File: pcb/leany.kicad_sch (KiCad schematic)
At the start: 40 parts, among them J1 ST7735S, J2 SWD, Q1 AO3401A, SW1 ZERO, SW2 HOLD, SW3 RESET, SW4 FLASH, U1 STM32F103C8Tx, U3 BMI270, U6 CH340N, Y1 8MHz

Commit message: add a reverse-voltage protection mosfet
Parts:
- U6: footprint leany_footprints:SOP-8_3.9x4.9mm_P1.27mm -> Package_SO:JEITA_SOIC-8_3.9x4.9mm_P1.27mm
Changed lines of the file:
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@@
 			)
 		)
-		(property "Footprint" "leany_footprints:SOP-8_3.9x4.9mm_P1.27mm"
+		(property "Footprint" "Package_SO:JEITA_SOIC-8_3.9x4.9mm_P1.27mm"
 			(at 214.63 97.79 0)
 			(effects
@@
 			)
 		)
-		(property "Description" "USB serial converter, 2Mbps, UART, SOP-8"
+		(property "Description" "USB serial converter, 2Mbps, UART, JEITA SOIC-8 (SOP-8)"
 			(at 210.82 116.84 0)
 			(effects

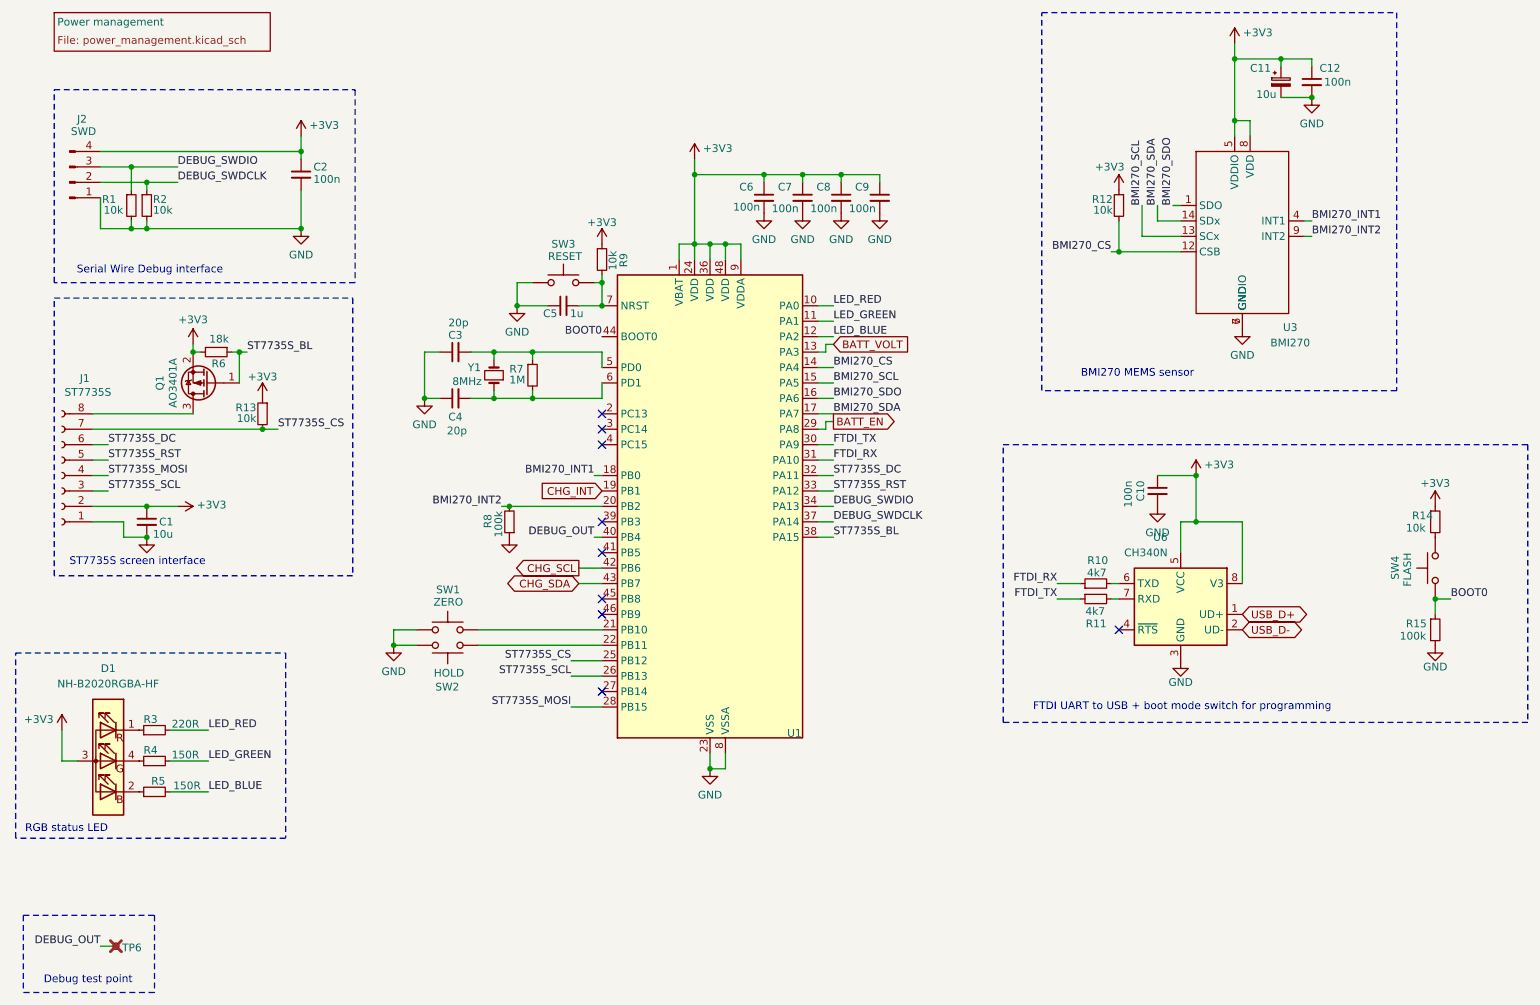
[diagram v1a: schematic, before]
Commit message: replace solder jumper by a test pad near battery
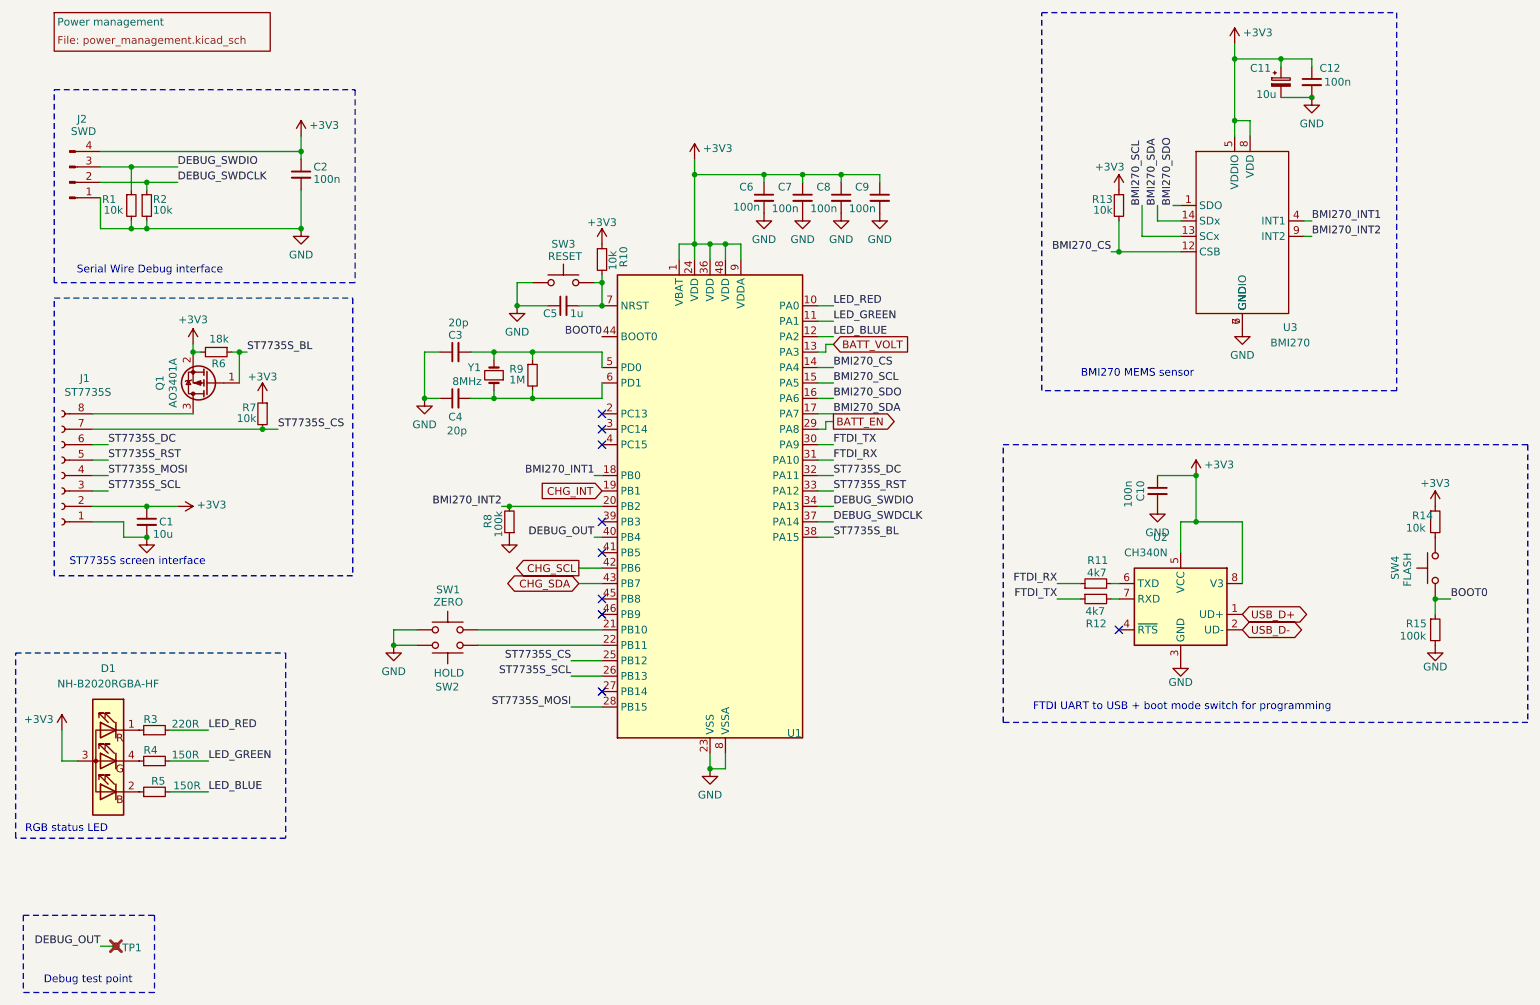
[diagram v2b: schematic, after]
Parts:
- U2: renamed from U6; footprint Package_SO:JEITA_SOIC-8_3.9x4.9mm_P1.27mm -> leany_footprints:SOP-8_3.9x4.9mm_P1.27mm
- renumbered R9 to R10, R10 to R11, R11 to R12, R12 to R13, R13 to R7, R7 to R9, TP6 to TP1
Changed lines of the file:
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@@
 		(on_board yes)
 		(dnp no)
-		(property "Reference" "#PWR06"
+		(property "Reference" "#PWR07"
 			(at 66.04 62.23 0)
 			(effects
@@
 			(project "leany"
 				(path "/e47b2519-93ca-4a48-9414-ecc253dd35f5"
-					(reference "#PWR06")
+					(reference "#PWR07")
 					(unit 1)
 				)
@@
 		(on_board yes)
 		(dnp no)
-		(property "Reference" "#PWR015"
+		(property "Reference" "#PWR016"
 			(at 148.59 59.69 0)
 			(effects
@@
 			(project "leany"
 				(path "/e47b2519-93ca-4a48-9414-ecc253dd35f5"
-					(reference "#PWR015")
+					(reference "#PWR016")
 					(unit 1)
 				)
@@
 		(on_board yes)
 		(dnp no)
-		(property "Reference" "#PWR014"
+		(property "Reference" "#PWR015"
 			(at 142.24 59.69 0)
 			(effects
@@
 			(project "leany"
 				(path "/e47b2519-93ca-4a48-9414-ecc253dd35f5"
-					(reference "#PWR014")
+					(reference "#PWR015")
 					(unit 1)
 				)
@@
 		(on_board yes)
 		(dnp no)
-		(property "Reference" "R12"
+		(property "Reference" "R13"
 			(at 199.644 51.054 0)
 			(effects
@@
 			(project "leany"
 				(path "/e47b2519-93ca-4a48-9414-ecc253dd35f5"
-					(reference "R12")
+					(reference "R13")
 					(unit 1)
 				)
@@
 		(on_board yes)
 		(dnp no)
-		(property "Reference" "#PWR021"
+		(property "Reference" "#PWR022"
 			(at 213.36 100.33 0)
 			(effects
@@
 			(project "leany"
 				(path "/e47b2519-93ca-4a48-9414-ecc253dd35f5"
-					(reference "#PWR021")
+					(reference "#PWR022")
 					(unit 1)
 				)
@@
 		(on_board yes)
 		(dnp no)
-		(property "Reference" "#PWR013"
+		(property "Reference" "#PWR014"
 			(at 133.35 151.13 0)
 			(effects
@@
 			(project ""
 				(path "/e47b2519-93ca-4a48-9414-ecc253dd35f5"
-					(reference "#PWR013")
+					(reference "#PWR014")
 					(unit 1)
 				)
@@
 		(on_board yes)
 		(dnp no)
-		(property "Reference" "#PWR05"
+		(property "Reference" "#PWR06"
 			(at 66.04 44.45 0)
 			(effects
@@
 			(project "leany"
 				(path "/e47b2519-93ca-4a48-9414-ecc253dd35f5"
-					(reference "#PWR05")
+					(reference "#PWR06")
 					(unit 1)
 				)
@@
 		(on_board yes)
 		(dnp no)
-		(property "Reference" "#PWR025"
+		(property "Reference" "#PWR026"
 			(at 252.73 105.41 0)
 			(effects
@@
 			(project "leany"
 				(path "/e47b2519-93ca-4a48-9414-ecc253dd35f5"
-					(reference "#PWR025")
+					(reference "#PWR026")
 					(unit 1)
 				)
@@
 		(on_board yes)
 		(dnp no)
-		(property "Reference" "#PWR018"
+		(property "Reference" "#PWR020"
 			(at 207.01 107.95 0)
 			(effects
@@
 			(project "leany"
 				(path "/e47b2519-93ca-4a48-9414-ecc253dd35f5"
-					(reference "#PWR018")
+					(reference "#PWR020")
 					(unit 1)
 				)
@@
 		(on_board yes)
 		(dnp no)
-		(property "Reference" "#PWR09"
+		(property "Reference" "#PWR011"
 			(at 101.6 74.93 0)
 			(effects
@@
 			(project "leany"
 				(path "/e47b2519-93ca-4a48-9414-ecc253dd35f5"
-					(reference "#PWR09")
+					(reference "#PWR011")
 					(unit 1)
 				)
@@
 		(on_board yes)
 		(dnp no)
-		(property "Reference" "R11"
+		(property "Reference" "R12"
 			(at 198.628 120.904 90)
 			(effects
@@
 			(project "leany"
 				(path "/e47b2519-93ca-4a48-9414-ecc253dd35f5"
-					(reference "R11")
+					(reference "R12")
 					(unit 1)
 				)
@@
 		(on_board yes)
 		(dnp no)
-		(property "Reference" "#PWR045"
+		(property "Reference" "#PWR05"
 			(at 59.69 87.63 0)
 			(effects
@@
 			(project "leany"
 				(path "/e47b2519-93ca-4a48-9414-ecc253dd35f5"
-					(reference "#PWR045")
+					(reference "#PWR05")
 					(unit 1)
 				)
@@
 		(on_board yes)
 		(dnp no)
-		(property "Reference" "#PWR016"
+		(property "Reference" "#PWR017"
 			(at 154.94 59.69 0)
 			(effects
@@
 			(project "leany"
 				(path "/e47b2519-93ca-4a48-9414-ecc253dd35f5"
-					(reference "#PWR016")
+					(reference "#PWR017")
 					(unit 1)
 				)
@@
 		(on_board yes)
 		(dnp no)
-		(property "Reference" "R13"
+		(property "Reference" "R7"
 			(at 58.674 85.344 0)
 			(effects
@@
 			(project "leany"
 				(path "/e47b2519-93ca-4a48-9414-ecc253dd35f5"
-					(reference "R13")
+					(reference "R7")
 					(unit 1)
 				)
@@
 		(on_board yes)
 		(dnp no)
-		(property "Reference" "#PWR07"
+		(property "Reference" "#PWR08"
 			(at 81.28 130.81 0)
 			(effects
@@
 			(project "leany"
 				(path "/e47b2519-93ca-4a48-9414-ecc253dd35f5"
-					(reference "#PWR07")
+					(reference "#PWR08")
 					(unit 1)
 				)
@@
 		(on_board yes)
 		(dnp no)
-		(property "Reference" "R9"
+		(property "Reference" "R10"
 			(at 119.126 62.23 90)
 			(effects
@@
 			(project "leany"
 				(path "/e47b2519-93ca-4a48-9414-ecc253dd35f5"
-					(reference "R9")
+					(reference "R10")
 					(unit 1)
 				)
@@
 		(on_board yes)
 		(dnp no)
-		(property "Reference" "R10"
+		(property "Reference" "R11"
 			(at 198.882 110.49 90)
 			(effects
@@
 			(project "leany"
 				(path "/e47b2519-93ca-4a48-9414-ecc253dd35f5"
-					(reference "R10")
+					(reference "R11")
 					(unit 1)
 				)
@@
 		(on_board yes)
 		(dnp no)
-		(property "Reference" "U6"
+		(property "Reference" "U2"
 			(at 208.6767 106.68 0)
 			(effects
@@
 			)
 		)
-		(property "Footprint" "Package_SO:JEITA_SOIC-8_3.9x4.9mm_P1.27mm"
+		(property "Footprint" "leany_footprints:SOP-8_3.9x4.9mm_P1.27mm"
 			(at 214.63 97.79 0)
 			(effects
@@
 			)
 		)
-		(property "Description" "USB serial converter, 2Mbps, UART, JEITA SOIC-8 (SOP-8)"
+		(property "Description" "USB serial converter, 2Mbps, UART, SOP-8"
 			(at 210.82 116.84 0)
 			(effects
@@
 			(project ""
 				(path "/e47b2519-93ca-4a48-9414-ecc253dd35f5"
-					(reference "U6")
+					(reference "U2")
 					(unit 1)
 				)
@@
 		(on_board yes)
 		(dnp no)
-		(property "Reference" "#PWR023"
+		(property "Reference" "#PWR024"
 			(at 220.98 78.74 0)
 			(effects
@@
 			(project "leany"
 				(path "/e47b2519-93ca-4a48-9414-ecc253dd35f5"
-					(reference "#PWR023")
+					(reference "#PWR024")
 					(unit 1)
 				)
@@
 		(on_board yes)
 		(dnp no)
-		(property "Reference" "R7"
+		(property "Reference" "R9"
 			(at 100.33 78.994 0)
 			(effects
@@
 			(project ""
 				(path "/e47b2519-93ca-4a48-9414-ecc253dd35f5"
-					(reference "R7")
+					(reference "R9")
 					(unit 1)
 				)
@@
 		(on_board yes)
 		(dnp no)
-		(property "Reference" "#PWR08"
+		(property "Reference" "#PWR09"
 			(at 86.36 90.17 0)
 			(effects
@@
 			(project "leany"
 				(path "/e47b2519-93ca-4a48-9414-ecc253dd35f5"
-					(reference "#PWR08")
+					(reference "#PWR09")
 					(unit 1)
 				)
@@
 		(on_board yes)
 		(dnp yes)
-		(property "Reference" "TP6"
+		(property "Reference" "TP1"
 			(at 36.576 174.244 90)
 			(effects
@@
 			(project "leany"
 				(path "/e47b2519-93ca-4a48-9414-ecc253dd35f5"
-					(reference "TP6")
+					(reference "TP1")
 					(unit 1)
 				)
@@
 		(on_board yes)
 		(dnp no)
-		(property "Reference" "#PWR012"
+		(property "Reference" "#PWR013"
 			(at 130.81 48.26 0)
 			(effects
@@
 			(project "leany"
 				(path "/e47b2519-93ca-4a48-9414-ecc253dd35f5"
-					(reference "#PWR012")
+					(reference "#PWR013")
 					(unit 1)
 				)
@@
 		(on_board yes)
 		(dnp no)
-		(property "Reference" "#PWR017"
+		(property "Reference" "#PWR018"
 			(at 161.29 59.69 0)
 			(effects
@@
 			(project "leany"
 				(path "/e47b2519-93ca-4a48-9414-ecc253dd35f5"
-					(reference "#PWR017")
+					(reference "#PWR018")
 					(unit 1)
 				)
@@
 		(on_board yes)
 		(dnp no)
-		(property "Reference" "#PWR020"
+		(property "Reference" "#PWR021"
 			(at 210.82 133.35 0)
 			(effects
@@
 			(project "leany"
 				(path "/e47b2519-93ca-4a48-9414-ecc253dd35f5"
-					(reference "#PWR020")
+					(reference "#PWR021")
 					(unit 1)
 				)
@@
 		(on_board yes)
 		(dnp no)
-		(property "Reference" "#PWR011"
+		(property "Reference" "#PWR012"
 			(at 115.57 62.23 0)
 			(effects
@@
 			(project "leany"
 				(path "/e47b2519-93ca-4a48-9414-ecc253dd35f5"
-					(reference "#PWR011")
+					(reference "#PWR012")
 					(unit 1)
 				)
@@
 		(on_board yes)
 		(dnp no)
-		(property "Reference" "#PWR022"
+		(property "Reference" "#PWR023"
 			(at 219.71 29.21 0)
 			(effects
@@
 			(project "leany"
 				(path "/e47b2519-93ca-4a48-9414-ecc253dd35f5"
-					(reference "#PWR022")
+					(reference "#PWR023")
 					(unit 1)
 				)
@@
 		(on_board yes)
 		(dnp no)
-		(property "Reference" "#PWR024"
+		(property "Reference" "#PWR025"
 			(at 232.41 40.64 0)
 			(effects
@@
 			(project "leany"
 				(path "/e47b2519-93ca-4a48-9414-ecc253dd35f5"
-					(reference "#PWR024")
+					(reference "#PWR025")
 					(unit 1)
 				)
@@
 		(on_board yes)
 		(dnp no)
-		(property "Reference" "#PWR026"
+		(property "Reference" "#PWR027"
 			(at 252.73 130.81 0)
 			(effects
@@
 			(project "leany"
 				(path "/e47b2519-93ca-4a48-9414-ecc253dd35f5"
-					(reference "#PWR026")
+					(reference "#PWR027")
 					(unit 1)
 				)

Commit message: start re-designing PCB to 4 layers
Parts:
- C10, C12, C2, C3, C4, C5, C6, C7, C8, C9: footprint Capacitor_SMD:C_0603_1608Metric -> Capacitor_SMD:C_0402_1005Metric
- R1, R10, R11, R12, R13, R14, R15, R2, R3, R4, R5, R6, R7, R8, R9: footprint Resistor_SMD:R_0603_1608Metric -> Resistor_SMD:R_0402_1005Metric
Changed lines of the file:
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@@
 			)
 		)
-		(property "Footprint" "Resistor_SMD:R_0603_1608Metric"
+		(property "Footprint" "Resistor_SMD:R_0402_1005Metric"
 			(at 252.73 121.92 0)
 			(effects
@@
 			)
 		)
-		(property "Footprint" "Capacitor_SMD:C_0603_1608Metric"
+		(property "Footprint" "Capacitor_SMD:C_0402_1005Metric"
 			(at 161.29 50.8 0)
 			(effects
@@
 			)
 		)
-		(property "Footprint" "Resistor_SMD:R_0603_1608Metric"
+		(property "Footprint" "Resistor_SMD:R_0402_1005Metric"
 			(at 41.91 148.59 0)
 			(effects
@@
 			)
 		)
-		(property "Footprint" "Resistor_SMD:R_0603_1608Metric"
+		(property "Footprint" "Resistor_SMD:R_0402_1005Metric"
 			(at 38.1 52.07 0)
 			(effects
@@
 			)
 		)
-		(property "Footprint" "Resistor_SMD:R_0603_1608Metric"
+		(property "Footprint" "Resistor_SMD:R_0402_1005Metric"
 			(at 40.64 52.07 0)
 			(effects
@@
 			)
 		)
-		(property "Footprint" "Resistor_SMD:R_0603_1608Metric"
+		(property "Footprint" "Resistor_SMD:R_0402_1005Metric"
 			(at 200.66 52.07 0)
 			(effects
@@
 			)
 		)
-		(property "Footprint" "Capacitor_SMD:C_0603_1608Metric"
+		(property "Footprint" "Capacitor_SMD:C_0402_1005Metric"
 			(at 91.44 83.82 0)
 			(effects
@@
 			)
 		)
-		(property "Footprint" "Capacitor_SMD:C_0603_1608Metric"
+		(property "Footprint" "Capacitor_SMD:C_0402_1005Metric"
 			(at 66.04 46.99 0)
 			(effects
@@
 			)
 		)
-		(property "Footprint" "Capacitor_SMD:C_0603_1608Metric"
+		(property "Footprint" "Capacitor_SMD:C_0402_1005Metric"
 			(at 232.41 31.75 0)
 			(effects
@@
 			)
 		)
-		(property "Footprint" "Resistor_SMD:R_0603_1608Metric"
+		(property "Footprint" "Resistor_SMD:R_0402_1005Metric"
 			(at 41.91 143.51 0)
 			(effects
@@
 			)
 		)
-		(property "Footprint" "Resistor_SMD:R_0603_1608Metric"
+		(property "Footprint" "Resistor_SMD:R_0402_1005Metric"
 			(at 252.73 104.14 0)
 			(effects
@@
 			)
 		)
-		(property "Footprint" "Resistor_SMD:R_0603_1608Metric"
+		(property "Footprint" "Resistor_SMD:R_0402_1005Metric"
 			(at 196.85 116.84 0)
 			(effects
@@
 			)
 		)
-		(property "Footprint" "Resistor_SMD:R_0603_1608Metric"
+		(property "Footprint" "Resistor_SMD:R_0402_1005Metric"
 			(at 59.69 86.36 0)
 			(effects
@@
 			)
 		)
-		(property "Footprint" "Resistor_SMD:R_0603_1608Metric"
+		(property "Footprint" "Resistor_SMD:R_0402_1005Metric"
 			(at 52.07 76.2 0)
 			(effects
@@
 			)
 		)
-		(property "Footprint" "Resistor_SMD:R_0603_1608Metric"
+		(property "Footprint" "Resistor_SMD:R_0402_1005Metric"
 			(at 115.57 60.96 0)
 			(effects
@@
 			)
 		)
-		(property "Footprint" "Resistor_SMD:R_0603_1608Metric"
+		(property "Footprint" "Resistor_SMD:R_0402_1005Metric"
 			(at 196.85 114.3 0)
 			(effects
@@
 			)
 		)
-		(property "Footprint" "Capacitor_SMD:C_0603_1608Metric"
+		(property "Footprint" "Capacitor_SMD:C_0402_1005Metric"
 			(at 109.22 68.58 0)
 			(effects
@@
 			)
 		)
-		(property "Footprint" "Resistor_SMD:R_0603_1608Metric"
+		(property "Footprint" "Resistor_SMD:R_0402_1005Metric"
 			(at 104.14 80.01 0)
 			(effects
@@
 			)
 		)
-		(property "Footprint" "Resistor_SMD:R_0603_1608Metric"
+		(property "Footprint" "Resistor_SMD:R_0402_1005Metric"
 			(at 41.91 138.43 0)
 			(effects
@@
 			)
 		)
-		(property "Footprint" "Capacitor_SMD:C_0603_1608Metric"
+		(property "Footprint" "Capacitor_SMD:C_0402_1005Metric"
 			(at 154.94 50.8 0)
 			(effects
@@
 			)
 		)
-		(property "Footprint" "Capacitor_SMD:C_0603_1608Metric"
+		(property "Footprint" "Capacitor_SMD:C_0402_1005Metric"
 			(at 91.44 76.2 0)
 			(effects
@@
 			)
 		)
-		(property "Footprint" "Capacitor_SMD:C_0603_1608Metric"
+		(property "Footprint" "Capacitor_SMD:C_0402_1005Metric"
 			(at 142.24 50.8 0)
 			(effects
@@
 			)
 		)
-		(property "Footprint" "Capacitor_SMD:C_0603_1608Metric"
+		(property "Footprint" "Capacitor_SMD:C_0402_1005Metric"
 			(at 148.59 50.8 0)
 			(effects
@@
 			)
 		)
-		(property "Footprint" "Resistor_SMD:R_0603_1608Metric"
+		(property "Footprint" "Resistor_SMD:R_0402_1005Metric"
 			(at 100.33 104.14 0)
 			(effects
@@
 			)
 		)
-		(property "Footprint" "Capacitor_SMD:C_0603_1608Metric"
+		(property "Footprint" "Capacitor_SMD:C_0402_1005Metric"
 			(at 207.01 99.06 0)
 			(effects

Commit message: start placing components
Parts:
- added C25, C26: 100n, Capacitor_SMD:C_0402_1005Metric, symbol Device:C_Small
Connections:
- net +3V3: now also C25.1, C26.1
- net GND: now also C25.2, C26.2

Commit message: update resistors BOM
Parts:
- R1, R10, R13, R14, R2, R7: LCSC C25804 -> C25744
- R11, R12: LCSC C23162 -> C25900
- R15, R8: LCSC C25803 -> C25741
- R3: LCSC C22962 -> C25091
- R4, R5, R6: footprint Resistor_SMD:R_0402_1005Metric -> Resistor_SMD:R_0603_1608Metric
- R9: LCSC C22935 -> C26083
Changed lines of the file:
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@@
 			)
 		)
-		(property "LCSC" "C25803"
+		(property "LCSC" "C25741"
 			(at 252.73 121.92 0)
 			(effects
@@
 			)
 		)
-		(property "Footprint" "Resistor_SMD:R_0402_1005Metric"
+		(property "Footprint" "Resistor_SMD:R_0603_1608Metric"
 			(at 41.91 148.59 0)
 			(effects
@@
 			)
 		)
-		(property "LCSC" "C25804"
+		(property "LCSC" "C25744"
 			(at 38.1 52.07 0)
 			(effects
@@
 			)
 		)
-		(property "LCSC" "C25804"
+		(property "LCSC" "C25744"
 			(at 40.64 52.07 0)
 			(effects
@@
 			)
 		)
-		(property "LCSC" "C25804"
+		(property "LCSC" "C25744"
 			(at 200.66 52.07 0)
 			(effects
@@
 			)
 		)
-		(property "Footprint" "Resistor_SMD:R_0402_1005Metric"
+		(property "Footprint" "Resistor_SMD:R_0603_1608Metric"
 			(at 41.91 143.51 0)
 			(effects
@@
 			)
 		)
-		(property "LCSC" "C25804"
+		(property "LCSC" "C25744"
 			(at 252.73 104.14 0)
 			(effects
@@
 			)
 		)
-		(property "LCSC" "C23162"
+		(property "LCSC" "C25900"
 			(at 196.85 116.84 0)
 			(effects
@@
 			)
 		)
-		(property "LCSC" "C25804"
+		(property "LCSC" "C25744"
 			(at 59.69 86.36 0)
 			(effects
@@
 			)
 		)
-		(property "Footprint" "Resistor_SMD:R_0402_1005Metric"
+		(property "Footprint" "Resistor_SMD:R_0603_1608Metric"
 			(at 52.07 76.2 0)
 			(effects
@@
 			)
 		)
-		(property "LCSC" "C25804"
+		(property "LCSC" "C25744"
 			(at 115.57 60.96 0)
 			(effects
@@
 			)
 		)
-		(property "LCSC" "C23162"
+		(property "LCSC" "C25900"
 			(at 196.85 114.3 0)
 			(effects
@@
 			)
 		)
-		(property "LCSC" "C22935"
+		(property "LCSC" "C26083"
 			(at 104.14 80.01 0)
 			(effects
@@
 			)
 		)
-		(property "LCSC" "C22962"
+		(property "LCSC" "C25091"
 			(at 41.91 138.43 0)
 			(effects
@@
 			)
 		)
-		(property "LCSC" "C25803"
+		(property "LCSC" "C25741"
 			(at 100.33 104.14 0)
 			(effects
